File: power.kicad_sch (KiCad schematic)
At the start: 60 parts, among them U1 TPS56A37RPAR, U3 LM3881MM, U4 TPS62823DLC, U5 TPS62823DLC, U6 TPS62823DLC, U7 TPS62823DLC, U8 TPS62823DLC

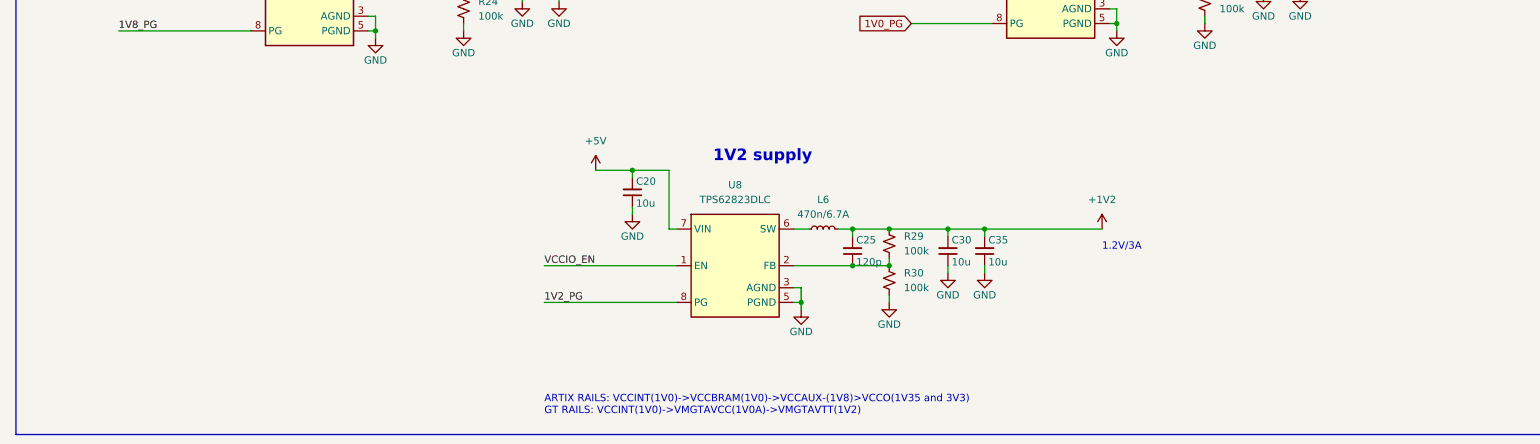
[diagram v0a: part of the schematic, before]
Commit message: added adc
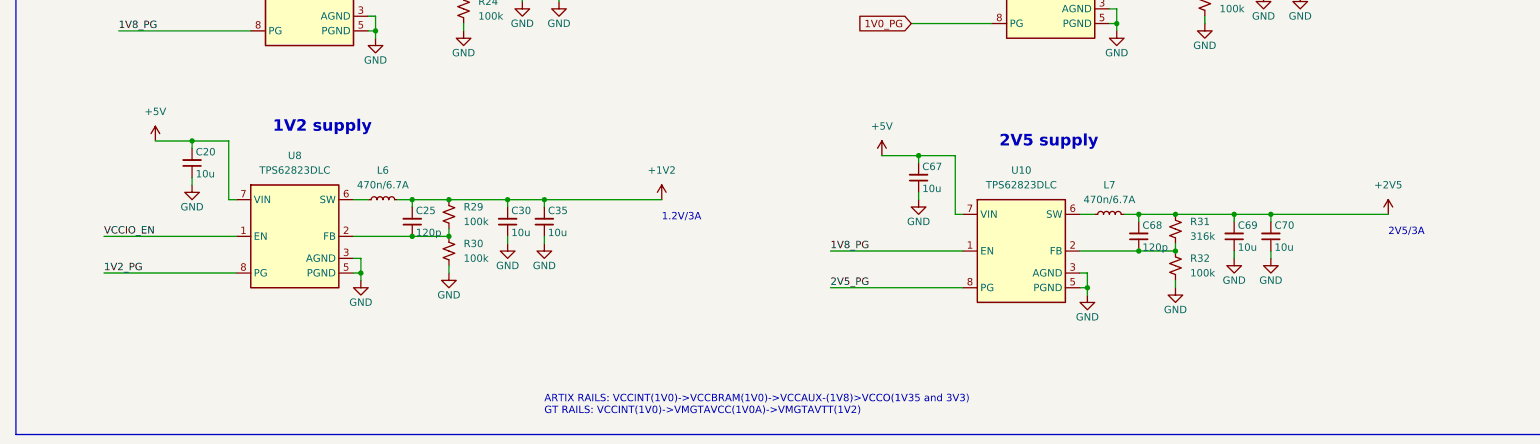
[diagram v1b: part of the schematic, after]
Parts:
- added C67: 10uF, Capacitor_SMD:C_0603_1608Metric, symbol antmicroCapacitors0603:C_10u_0603
- added C68: 120pF, Capacitor_SMD:C_0402_1005Metric, symbol antmicroCapacitors0402:C_120p_0402
- added C69, C70: 10uF, Capacitor_SMD:C_0402_1005Metric, symbol antmicroCapacitors0402:C_10u_0402
- added L7: WTXE322512TR47MT, Inductor_SMD:L_1210_3225Metric_Pad1.42x2.65mm_HandSolder, symbol antmicroFixedInductors:IHLP1212AEERR47M11
- added R31: 316k, Resistor_SMD:R_0402_1005Metric, symbol Device:R_Small_US
- added R32: 100k, Resistor_SMD:R_0402_1005Metric, symbol Device:R_Small_US
- added U10: TPS62823DLC, Package_SON:Texas_VSON-HR-8_1.5x2mm_P0.5mm, symbol Regulator_Switching:TPS62823DLC
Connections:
- net +5V: now also C67.2, U10.7 (VIN)
- net 1V8_PG: now also U10.1 (EN)
- net GND: now also C67.1, C69.1, C70.1, R32.2, U10.3 (AGND), U10.5 (PGND)
- new net: C68.1, R31.2, R32.1, U10.2 (FB)
- new net: L7.1, U10.6 (SW)
- new net +2V5: C68.2, C69.2, C70.2, L7.2, R31.1
- new net 2V5_PG: U10.8 (PG)
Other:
- note added: "2V5 supply"
- note added: "2V5/3A"
- moved on the sheet: C20, C25, C30, C35, L6, R29, R30, U8

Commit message: added clk
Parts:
- added C71, C72: 4.7uF, Capacitor_SMD:C_0402_1005Metric, symbol Device:C_Small
- added C75: 10uF, Capacitor_SMD:C_0603_1608Metric, symbol antmicroCapacitors0603:C_10u_0603
- added C76: 120pF, Capacitor_SMD:C_0402_1005Metric, symbol antmicroCapacitors0402:C_120p_0402
- added C77, C78: 10uF, Capacitor_SMD:C_0402_1005Metric, symbol antmicroCapacitors0402:C_10u_0402
- added C79: 10n, Capacitor_SMD:C_0603_1608Metric, symbol antmicroCapacitors0603:C_10u_0603
- added L9: WTXE322512TR47MT, Inductor_SMD:L_1210_3225Metric_Pad1.42x2.65mm_HandSolder, symbol antmicroFixedInductors:IHLP1212AEERR47M11
- added R35: 316k, Resistor_SMD:R_0402_1005Metric, symbol Device:R_Small_US
- added R36: 100k, Resistor_SMD:R_0402_1005Metric, symbol Device:R_Small_US
- added U12: ADP1740ACPZ-1.8-R7, CP_16_23_ADI, symbol ADP1740ACPZ-1.8-R7:ADP1740ACPZ-1.8-R7
- added U13: TPS62823DLC, Package_SON:Texas_VSON-HR-8_1.5x2mm_P0.5mm, symbol Regulator_Switching:TPS62823DLC
- C1: value 15uF -> 15u
- C2: value 1uF -> 1u
- C3: value 22nF -> 22n
- C4: value 100nF -> 100n
- C5: value 150pF -> 150p
- C6, C7: value 22uF -> 22u
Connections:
- net +5V: now also C75.2, U13.7 (VIN)
- net 1V8_PG: now also U13.1 (EN)
- net 2V5_PG: now also U13.8 (PG)
- net GND: now also C71.2, C72.2, C75.1, C77.1, C78.1, C79.1, R36.2, U12.17 (EPAD), U12.6 (GND), U13.3 (AGND), U13.5 (PGND)
- new net: C76.1, R35.2, R36.1, U13.2 (FB)
- new net: L9.1, U13.6 (SW)
- new net: C79.2, U12.7 (SS)
- new net +1V8A: C71.1, U12.10 (VOUT), U12.11 (VOUT), U12.12 (VOUT), U12.13 (VOUT), U12.14 (VOUT), U12.9 (SENSE)
- new net +2V5A: C72.1, C76.2, C77.2, C78.2, L9.2, R35.1, U12.1 (VIN), U12.15 (VIN), U12.16 (VIN), U12.2 (VIN), U12.3 (VIN), U12.4 (EN)
- no-connect marks 1 -> 2
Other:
- note added: "1V8 supply (clean)"
- note added: "ADC Power"
